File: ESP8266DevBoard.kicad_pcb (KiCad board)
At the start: 2 copper layers, 105 x 60 mm, 0 parts

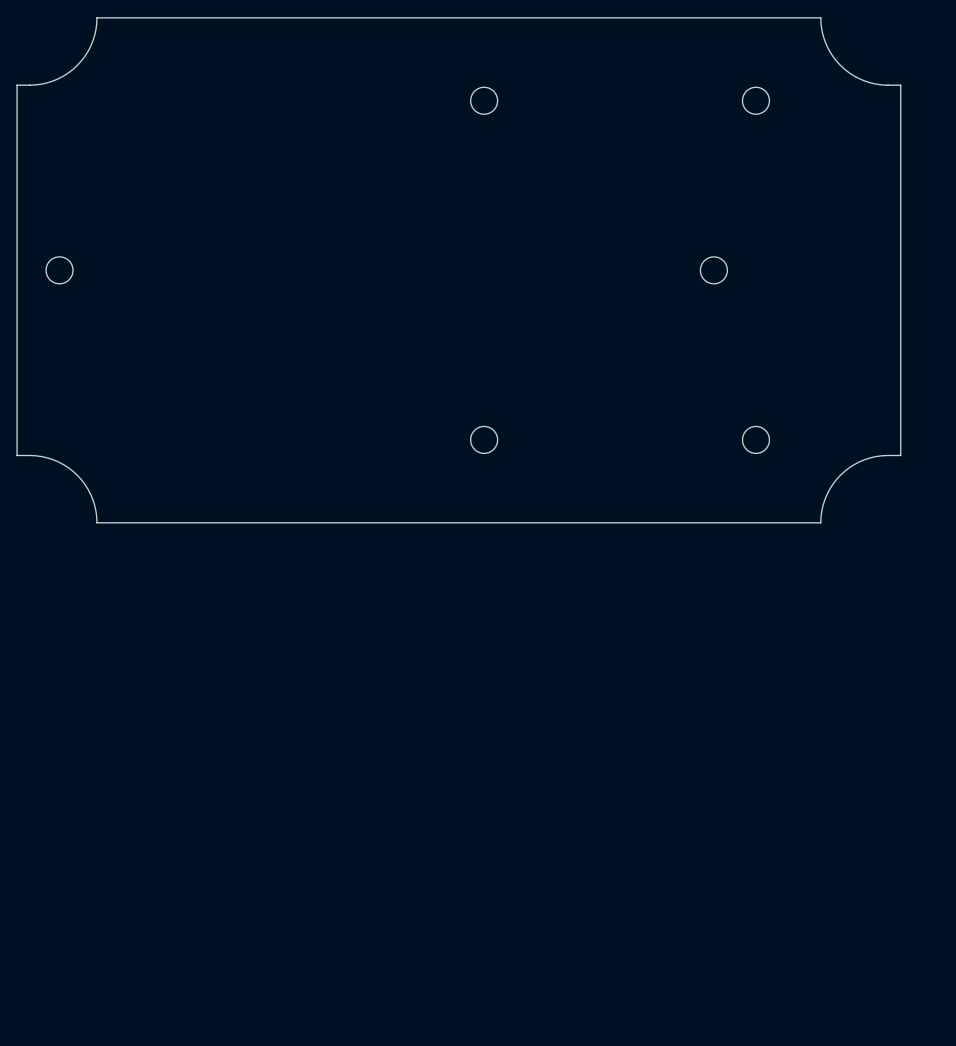
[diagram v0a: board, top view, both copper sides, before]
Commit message: 3mm LED added to schematic, footprints assigned.
Signed-off-by: Ion Bold <bold.ion86@gmail.com>
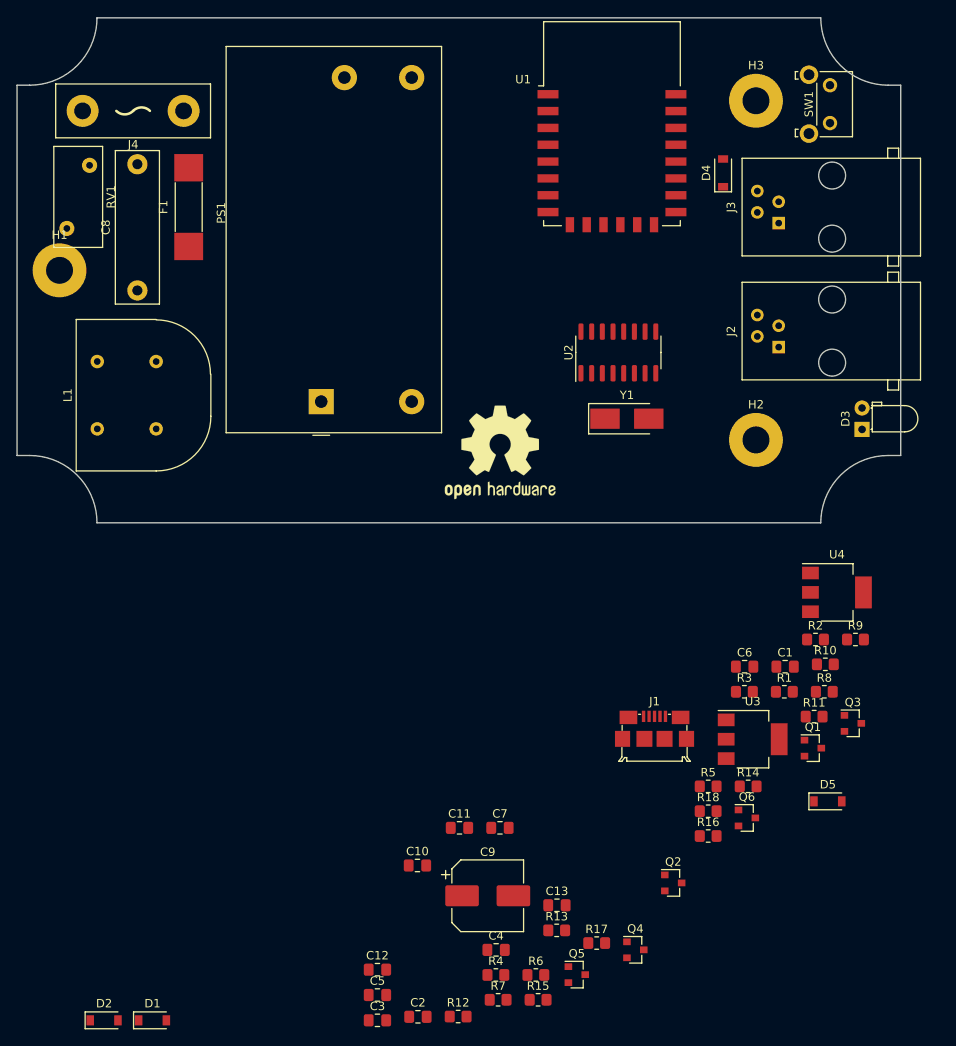
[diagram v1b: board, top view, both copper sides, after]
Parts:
- added C1: 10u, Capacitor_SMD:C_0805_2012Metric_Pad1.18x1.45mm_HandSolder, F.Cu at (191.3, 117.1)
- added C10: 100n, Capacitor_SMD:C_0805_2012Metric_Pad1.18x1.45mm_HandSolder, F.Cu at (147.6, 140.7)
- added C11: 10u, Capacitor_SMD:C_0805_2012Metric_Pad1.18x1.45mm_HandSolder, F.Cu at (152.6, 136.2)
- added C12: 100n, Capacitor_SMD:C_0805_2012Metric_Pad1.18x1.45mm_HandSolder, F.Cu at (142.8, 153.1)
- added C13: 10u, Capacitor_SMD:C_0805_2012Metric_Pad1.18x1.45mm_HandSolder, F.Cu at (164.2, 145.4)
- added C2: 100n, Capacitor_SMD:C_0805_2012Metric_Pad1.18x1.45mm_HandSolder, F.Cu at (147.6, 158.7)
- added C3: 100n, Capacitor_SMD:C_0805_2012Metric_Pad1.18x1.45mm_HandSolder, F.Cu at (142.8, 159.1)
- added C4: 100n, Capacitor_SMD:C_0805_2012Metric_Pad1.18x1.45mm_HandSolder, F.Cu at (156.9, 150.7)
- added C5: 10u, Capacitor_SMD:C_0805_2012Metric_Pad1.18x1.45mm_HandSolder, F.Cu at (142.8, 156.1)
- added C6: 18p, Capacitor_SMD:C_0805_2012Metric_Pad1.18x1.45mm_HandSolder, F.Cu at (186.5, 117.1)
- added C7: 18p, Capacitor_SMD:C_0805_2012Metric_Pad1.18x1.45mm_HandSolder, F.Cu at (157.4, 136.2)
- added C8: 0.1u/275Vac, Capacitor_THT:C_Rect_L18.0mm_W5.0mm_P15.00mm_FKS3_FKP3, F.Cu at (114.3, 72.4)
- added C9: 220u, Capacitor_SMD:CP_Elec_8x5.4, F.Cu at (155.9, 144.3)
- added D1: 1N5819HWQ-7-F, Diode_SMD:D_SOD-123, F.Cu at (116.1, 159.1)
- added D2: 1N5819HWQ-7-F, Diode_SMD:D_SOD-123, F.Cu at (110.3, 159.1)
- added D3: PWR, LED_THT:LED_D3.0mm_Horizontal_O1.27mm_Z2.0mm, F.Cu at (200.4, 88.9)
- added D4: 1N5819HWQ-7-F, Diode_SMD:D_SOD-123, F.Cu at (183.9, 58.4)
- added D5: 1N5819HWQ-7-F, Diode_SMD:D_SOD-123, F.Cu at (196.3, 133.1)
- added F1: 3405.0163.11, KiCadCustom:Fuse_10x3mm, F.Cu at (120.4, 62.5)
- added H1: MH, MountingHole:MountingHole_3.2mm_M3_Pad, F.Cu at (105.0, 70.0)
- added H2: MH, MountingHole:MountingHole_3.2mm_M3_Pad, F.Cu at (187.8, 90.2)
- added H3: MH, MountingHole:MountingHole_3.2mm_M3_Pad, F.Cu at (187.8, 49.9)
- added J1: 10118192-0001LF, KiCadCustom:USB_Micro-B_Amphenol_10118192-0001LF_Horizontal, F.Cu at (175.7, 125.7)
- added J2: RJ11-CHINA, KiCadCustom:RJ11_6P4C-2_54mm_Horizontal, F.Cu at (196.8, 77.2)
- added J3: RJ11-CHINA, KiCadCustom:RJ11_6P4C-2_54mm_Horizontal, F.Cu at (196.8, 62.5)
- added J4: AC, KiCadCustom:AC_Connector_2x2mm_P12mm, F.Cu at (113.8, 51.1)
- added L1: SU9H-01100, KiCadCustom:L_SU9H, F.Cu at (113.0, 84.8)
- added PS1: IRM-10-12, Converter_ACDC:Converter_ACDC_MeanWell_IRM-10-xx_THT, F.Cu at (136.1, 85.6)
- added Q1: BC847BLT1G, Package_TO_SOT_SMD:SOT-23, F.Cu at (194.6, 126.8)
- added Q2: BC847BLT1G, Package_TO_SOT_SMD:SOT-23, F.Cu at (178.0, 142.8)
- added Q3: BSS138, Package_TO_SOT_SMD:SOT-23, F.Cu at (199.3, 123.8)
- added Q4: BSS138, Package_TO_SOT_SMD:SOT-23, F.Cu at (173.5, 150.7)
- added Q5: BSS138, Package_TO_SOT_SMD:SOT-23, F.Cu at (166.5, 153.7)
- added Q6: BSS138, Package_TO_SOT_SMD:SOT-23, F.Cu at (186.7, 135.1)
- added R1: 10k, Resistor_SMD:R_0805_2012Metric_Pad1.20x1.40mm_HandSolder, F.Cu at (191.2, 120.1)
- added R10: 10k, Resistor_SMD:R_0805_2012Metric_Pad1.20x1.40mm_HandSolder, F.Cu at (196.0, 116.8)
- added R11: 10k, Resistor_SMD:R_0805_2012Metric_Pad1.20x1.40mm_HandSolder, F.Cu at (194.7, 123.0)
- added R12: 10k, Resistor_SMD:R_0805_2012Metric_Pad1.20x1.40mm_HandSolder, F.Cu at (152.4, 158.7)
- added R13: 10k, Resistor_SMD:R_0805_2012Metric_Pad1.20x1.40mm_HandSolder, F.Cu at (164.1, 148.4)
- added R14: 470R, Resistor_SMD:R_0805_2012Metric_Pad1.20x1.40mm_HandSolder, F.Cu at (186.9, 131.3)
- added R15: 10k, Resistor_SMD:R_0805_2012Metric_Pad1.20x1.40mm_HandSolder, F.Cu at (161.9, 156.7)
- added R16: 10k, Resistor_SMD:R_0805_2012Metric_Pad1.20x1.40mm_HandSolder, F.Cu at (182.1, 137.2)
- added R17: 10k, Resistor_SMD:R_0805_2012Metric_Pad1.20x1.40mm_HandSolder, F.Cu at (168.9, 149.9)
- added R18: 10k, Resistor_SMD:R_0805_2012Metric_Pad1.20x1.40mm_HandSolder, F.Cu at (182.1, 134.3)
- added R2: 10k, Resistor_SMD:R_0805_2012Metric_Pad1.20x1.40mm_HandSolder, F.Cu at (194.9, 113.9)
- added R3: 10k, Resistor_SMD:R_0805_2012Metric_Pad1.20x1.40mm_HandSolder, F.Cu at (186.4, 120.1)
- added R4: 10k, Resistor_SMD:R_0805_2012Metric_Pad1.20x1.40mm_HandSolder, F.Cu at (156.9, 153.7)
- added R5: 10k, Resistor_SMD:R_0805_2012Metric_Pad1.20x1.40mm_HandSolder, F.Cu at (182.1, 131.3)
- added R6: 10k, Resistor_SMD:R_0805_2012Metric_Pad1.20x1.40mm_HandSolder, F.Cu at (161.6, 153.7)
- added R7: 10k, Resistor_SMD:R_0805_2012Metric_Pad1.20x1.40mm_HandSolder, F.Cu at (157.2, 156.7)
- added R8: 470R, Resistor_SMD:R_0805_2012Metric_Pad1.20x1.40mm_HandSolder, F.Cu at (195.9, 120.1)
- added R9: 470R, Resistor_SMD:R_0805_2012Metric_Pad1.20x1.40mm_HandSolder, F.Cu at (199.6, 113.9)
- added REF**: OSHW-Logo2_14.6x12mm_SilkScreen, Symbol:OSHW-Logo2_14.6x12mm_SilkScreen, F.Cu at (157.4, 91.6)
- added RV1: MOV-10D561K, Varistor:RV_Disc_D12mm_W5.8mm_P7.5mm, F.Cu at (105.9, 65.0)
- added SW1: Switch_Push, KiCadCustom:SW_Tactile_SKHH_Angled, F.Cu at (196.6, 48.0)
- added U1: ESP-12F, RF_Module:ESP-12E, F.Cu at (170.7, 52.6)
- added U2: CH340G, Package_SO:SOIC-16_3.9x9.9mm_P1.27mm, F.Cu at (171.4, 79.8)
- added U3: LD1117S50TR, Package_TO_SOT_SMD:SOT-223-3_TabPin2, F.Cu at (187.4, 125.7)
- added U4: LD1117S33TR, Package_TO_SOT_SMD:SOT-223-3_TabPin2, F.Cu at (197.4, 108.3)
- added Y1: ABM3-12.000MHZ-D2Y-T, Crystal:Crystal_SMD_5032-2Pin_5.0x3.2mm_HandSoldering, F.Cu at (172.5, 87.6)
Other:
- outline, holes or cut-outs redrawn

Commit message: Components placed on the board.
Signed-off-by: Ion Bold <bold.ion86@gmail.com>
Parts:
- REF**: moved to B.Cu
- moved D2 114.4 mm to (186.4, 73.7), turned to 90 degrees
- moved C3 111.5 mm to (157.2, 48.5), turned to 180 degrees
- moved R4 100.3 mm to (182.1, 56.6), turned to 180 degrees
- moved R7 98.7 mm to (182.1, 61.2), turned to 180 degrees
- moved C2 96.2 mm to (157.2, 63.0), turned to 180 degrees
- moved R12 88.2 mm to (177.5, 74.2), turned to 270 degrees
- moved R15 87.3 mm to (168.4, 69.6), turned to 270 degrees
- moved Q5 84.1 mm to (165.1, 69.6)
- moved D1 79.2 mm to (156.5, 90.9), turned to 270 degrees
- moved Q4 76.6 mm to (174.2, 74.2)
- moved R17 75.8 mm to (168.4, 74.2), turned to 270 degrees
- moved R6 75.6 mm to (170.9, 78.7), turned to 90 degrees
- moved R3 75.2 mm to (157.2, 50.8)
- moved R1 75.1 mm to (157.2, 53.1)
- moved R13 74.6 mm to (170.9, 74.2), turned to 270 degrees
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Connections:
- C3 pad 1: Net-(C3-Pad1) -> RST
- H1 pad 1: GND -> (no net)
- R3 pad 2: Net-(C3-Pad1) -> RST

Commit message: Routing done.
Signed-off-by: Ion Bold <bold.ion86@gmail.com>
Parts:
- moved REF** 29.3 mm to (142.0, 65.0)
- moved C8 15.2 mm to (110.7, 62.5), turned to 0 degrees
- moved RV1 8.03 mm to (114.6, 68.6), turned to 0 degrees
- moved F1 7.37 mm to (114.6, 84.1)
- moved J4 6.10 mm to (121.2, 84.1)
- moved C1 4.57 mm to (157.2, 60.7)
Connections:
- L1 pad 1: Net-(C8-Pad1) -> Net-(C8-Pad2)
- L1 pad 3: Net-(C8-Pad2) -> Net-(C8-Pad1)
- PS1 pad 1: Net-(L1-Pad4) -> Net-(L1-Pad2)
- PS1 pad 2: Net-(L1-Pad2) -> Net-(L1-Pad4)
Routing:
- net +3V3: track 0.00 -> 137.5 mm, vias 0 -> 3
- net RST: track 0.00 -> 97.6 mm, vias 0 -> 2
- net +5V: track 0.00 -> 92.1 mm, vias 0 -> 2
- net +12V: track 0.00 -> 91.0 mm, vias 0 -> 2
- net Net-(R9-Pad1): track 0.00 -> 79.1 mm, vias 0 -> 2
- net Net-(R8-Pad1): track 0.00 -> 76.8 mm, vias 0 -> 2
- net DATA1_1: track 0.00 -> 47.1 mm, vias 0 -> 2
- net GPIO0: track 0.00 -> 46.3 mm, vias 0 -> 2
- net DATA0_1: track 0.00 -> 41.4 mm, vias 0 -> 2
- net Net-(J3-Pad3): track 0.00 -> 36.9 mm, vias 0 -> 1
- net Net-(J3-Pad2): track 0.00 -> 36.8 mm, vias 0 -> 1
- net GND: track 0.00 -> 27.2 mm, vias 0 -> 12
- net Net-(L1-Pad2): track 0.00 -> 27.0 mm
- net Net-(C8-Pad1): track 0.00 -> 26.9 mm
- net Net-(C8-Pad2): track 0.00 -> 25.8 mm
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- added copper zone on B.Cu, net GND
- added copper zone on F.Cu, net GND
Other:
- board text added: "1"
- board text added: "2"

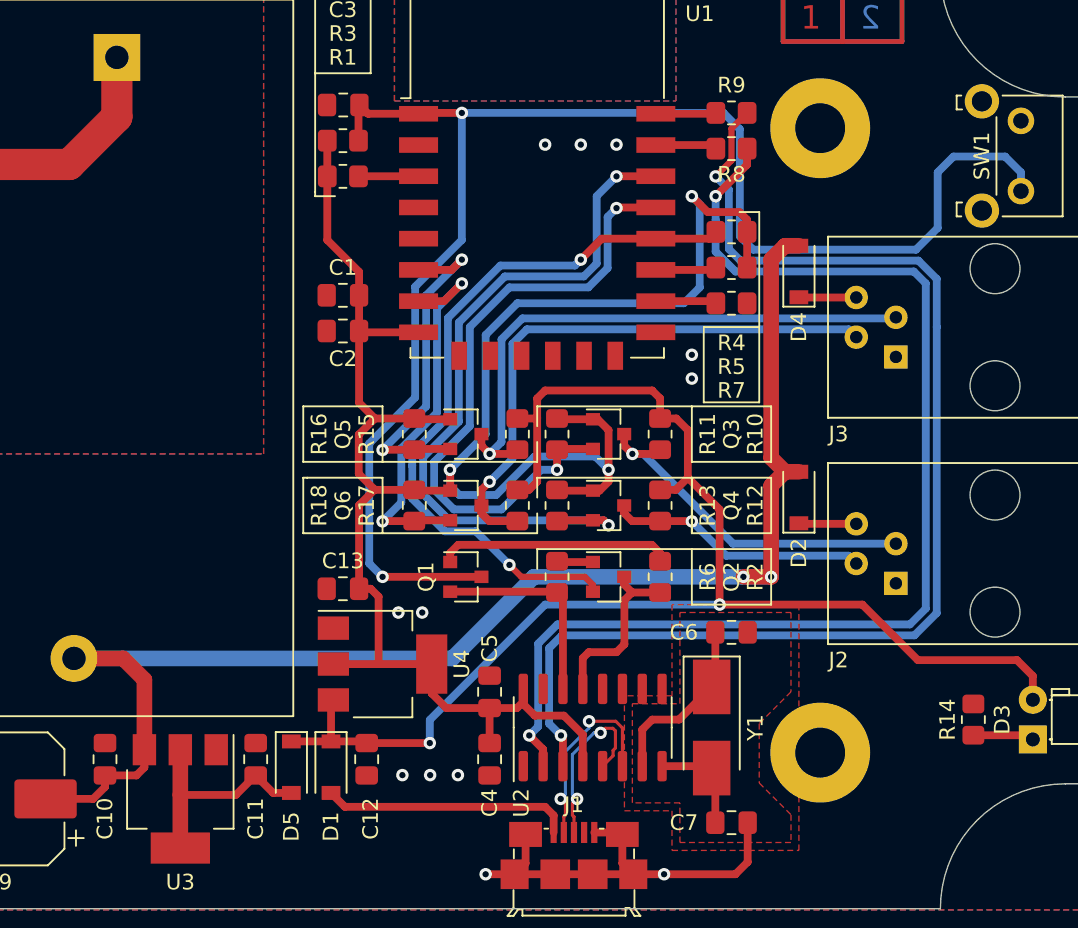
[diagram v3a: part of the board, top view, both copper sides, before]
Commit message: PCB routing done, gerber files added.
Signed-off-by: Ion Bold <bold.ion86@gmail.com>
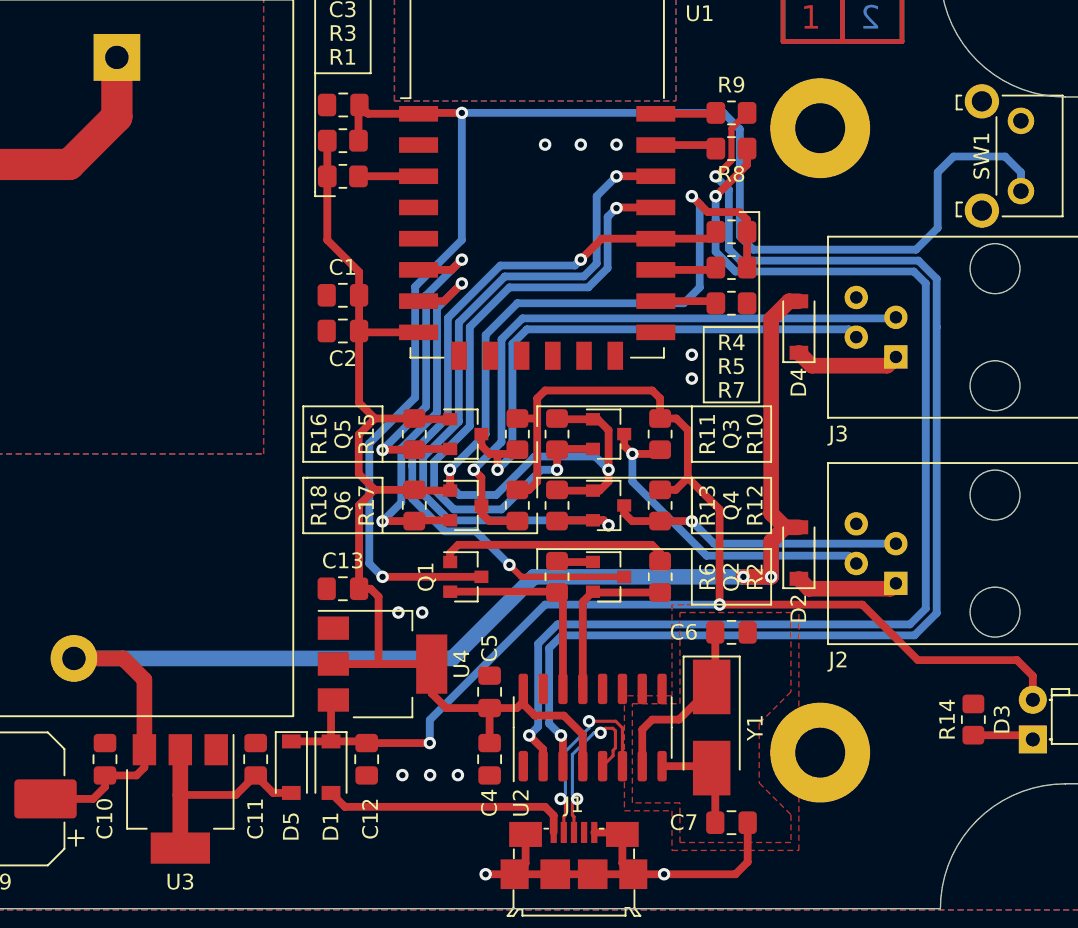
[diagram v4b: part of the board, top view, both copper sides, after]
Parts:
- Q3, Q4, Q5, Q6: value BSS138 -> 2N7002H6327XTSA2
- SW1: value Switch_Push -> B3F-3152
- moved D2 3.56 mm to (186.4, 77.2)
- moved D4 3.56 mm to (186.4, 62.7)
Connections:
- J2 pad 1: GND -> Net-(D2-Pad1)
- J2 pad 4: Net-(D2-Pad1) -> GND
- J3 pad 1: GND -> Net-(D4-Pad1)
- J3 pad 4: Net-(D4-Pad1) -> GND
- Q2 pad 2: GPIO0 -> DTR
- Q2 pad 3: DTR -> GPIO0
- Q3 pad 3: Net-(J2-Pad3) -> Net-(J2-Pad2)
- Q4 pad 3: Net-(J2-Pad2) -> Net-(J2-Pad3)
- Q5 pad 3: Net-(J3-Pad3) -> Net-(J3-Pad2)
- Q6 pad 3: Net-(J3-Pad2) -> Net-(J3-Pad3)
- R10 pad 2: Net-(J2-Pad3) -> Net-(J2-Pad2)
- R12 pad 2: Net-(J2-Pad2) -> Net-(J2-Pad3)
- R15 pad 2: Net-(J3-Pad3) -> Net-(J3-Pad2)
- R17 pad 2: Net-(J3-Pad2) -> Net-(J3-Pad3)
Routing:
- net Net-(J2-Pad2): track 16.7 -> 21.7 mm
- net Net-(J2-Pad3): track 22.7 -> 18.8 mm
- net +12V: track 91.0 -> 87.3 mm
- net Net-(J3-Pad3): track 36.9 -> 40.4 mm
- net Net-(D4-Pad1): track 3.68 -> 6.79 mm
- net Net-(D2-Pad1): track 3.69 -> 6.62 mm
- net GPIO0: track 46.3 -> 47.6 mm
- net Net-(J3-Pad2): track 36.8 -> 35.5 mm
- net DTR: track 11.5 -> 10.8 mm
